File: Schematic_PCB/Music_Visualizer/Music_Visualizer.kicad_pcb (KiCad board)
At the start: 2 copper layers, 295 x 155 mm, 257 parts, among them J1 AudioJack3, J2 PJ-079BH, J3 Screw_Terminal_01x02, Q1 DMP2123LQ-7, SW1 SW_SPDT, SW2 SW_SPST, U1 LM324, U10 LM3915N-1, U11 LM3915N-1, U12 LM3915N-1, U13 LM3915N-1, U14 LM3915N-1, U15 LM3915N-1, U16 LM3915N-1, U17 NCP161ASN350T1G, U18 NCS333ASQ3T2G, U2 LM324, U3 LM324, U4 LM324, U5 LM324, U6 LM324, U7 LM324, U8 LT1054, U9 MC78L05_TO92

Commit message: PCB LEDs placed
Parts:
- removed C1, C2: 47n, Capacitor_SMD:C_0603_1608Metric_Pad1.08x0.95mm_HandSolder
- removed C10, C9: 6.8n, Capacitor_SMD:C_0805_2012Metric
- removed C11, C12: 24n, Capacitor_SMD:C_0805_2012Metric
- removed C13, C14: 4.7n, Capacitor_SMD:C_0603_1608Metric_Pad1.08x0.95mm_HandSolder
- removed C15, C16: 3.3n, Capacitor_SMD:C_0603_1608Metric_Pad1.08x0.95mm_HandSolder
- removed C17, C18: 6.2n, Capacitor_SMD:C_0805_2012Metric
- removed C19, C20: 1.6n, Capacitor_SMD:C_0603_1608Metric_Pad1.08x0.95mm_HandSolder
- removed C21, C22, C25, C26, C27, C28, C29, C30, C31, C32, C33, C34, C35, C36, C37, C38, C41, C42: 1n, Capacitor_SMD:C_0603_1608Metric_Pad1.08x0.95mm_HandSolder
- removed C23, C24: 3n, Capacitor_SMD:C_0603_1608Metric_Pad1.08x0.95mm_HandSolder
- removed C3, C4: 27n, Capacitor_SMD:C_0603_1608Metric_Pad1.08x0.95mm_HandSolder
- removed C39, C40: 820p, Capacitor_SMD:C_0603_1608Metric_Pad1.08x0.95mm_HandSolder
- removed C5, C6: 75n, Capacitor_SMD:C_1206_3216Metric
- removed C59: 10u, Capacitor_THT:CP_Radial_D5.0mm_P2.00mm
- removed C60, C61, C62, C63, C64, C65, C66, C67, C68, C69, C70, C71, C72, C73: 0.1uF, Capacitor_SMD:C_0805_2012Metric
- removed C7, C8: 13n, Capacitor_SMD:C_0805_2012Metric
- removed J2: PJ-079BH, DC_Power_Jack_PJ_070BH:CUI_PJ-079BH
- removed R1: 84.5k, Resistor_SMD:R_0603_1608Metric_Pad0.98x0.95mm_HandSolder
- removed R10: 110k, Resistor_SMD:R_0603_1608Metric_Pad0.98x0.95mm_HandSolder
- removed R11, R4, R65: 90.9k, Resistor_SMD:R_0603_1608Metric_Pad0.98x0.95mm_HandSolder
- removed R12: 162k, Resistor_SMD:R_0603_1608Metric_Pad0.98x0.95mm_HandSolder
- removed R13: 118k, Resistor_SMD:R_0603_1608Metric_Pad0.98x0.95mm_HandSolder
- removed R14: 63.4k, Resistor_SMD:R_0603_1608Metric_Pad0.98x0.95mm_HandSolder
- removed R15: 62k, Resistor_SMD:R_0603_1608Metric_Pad0.98x0.95mm_HandSolder
- removed R16: 309k, Resistor_SMD:R_0603_1608Metric_Pad0.98x0.95mm_HandSolder
- removed R17: 68k, Resistor_SMD:R_0603_1608Metric_Pad0.98x0.95mm_HandSolder
- removed R18, R31, R36, R51: 66.5k, Resistor_SMD:R_0603_1608Metric_Pad0.98x0.95mm_HandSolder
- removed R19: 332k, Resistor_SMD:R_0603_1608Metric_Pad0.98x0.95mm_HandSolder
- removed R2, R41, R50: 160k, Resistor_SMD:R_0603_1608Metric_Pad0.98x0.95mm_HandSolder
- removed R20: 137k, Resistor_SMD:R_0603_1608Metric_Pad0.98x0.95mm_HandSolder
- removed R21: 45.3k, Resistor_SMD:R_0603_1608Metric_Pad0.98x0.95mm_HandSolder
- removed R22, R35, R53: 270k, Resistor_SMD:R_0603_1608Metric_Pad0.98x0.95mm_HandSolder
- removed R23: 143k, Resistor_SMD:R_0603_1608Metric_Pad0.98x0.95mm_HandSolder
- removed R24: 19.1k, Resistor_SMD:R_0603_1608Metric_Pad0.98x0.95mm_HandSolder
- removed R25: 590k, Resistor_SMD:R_0603_1608Metric_Pad0.98x0.95mm_HandSolder
- removed R26: 140k, Resistor_SMD:R_0603_1608Metric_Pad0.98x0.95mm_HandSolder
- removed R27: 18.7k, Resistor_SMD:R_0603_1608Metric_Pad0.98x0.95mm_HandSolder
- removed R28: 576k, Resistor_SMD:R_0603_1608Metric_Pad0.98x0.95mm_HandSolder
- removed R29, R30: 100k, Resistor_SMD:R_0603_1608Metric_Pad0.98x0.95mm_HandSolder
- removed R3: 169k, Resistor_SMD:R_0603_1608Metric_Pad0.98x0.95mm_HandSolder
- removed R32: 33.2k, Resistor_SMD:R_0603_1608Metric_Pad0.98x0.95mm_HandSolder
- removed R33: 56k, Resistor_SMD:R_0603_1608Metric_Pad0.98x0.95mm_HandSolder
- removed R34, R58: 48.7k, Resistor_SMD:R_0603_1608Metric_Pad0.98x0.95mm_HandSolder
- removed R37: 57.6k, Resistor_SMD:R_0603_1608Metric_Pad0.98x0.95mm_HandSolder
- removed R38: 324k, Resistor_SMD:R_0603_1608Metric_Pad0.98x0.95mm_HandSolder
- removed R39, R48: 78.7k, Resistor_SMD:R_0603_1608Metric_Pad0.98x0.95mm_HandSolder
- removed R40: 26.7k, Resistor_SMD:R_0603_1608Metric_Pad0.98x0.95mm_HandSolder
- removed R42: 59k, Resistor_SMD:R_0603_1608Metric_Pad0.98x0.95mm_HandSolder
- removed R43: 7.87k, Resistor_SMD:R_0603_1608Metric_Pad0.98x0.95mm_HandSolder
- removed R44: 243k, Resistor_SMD:R_0603_1608Metric_Pad0.98x0.95mm_HandSolder
- removed R45: 107k, Resistor_SMD:R_0603_1608Metric_Pad0.98x0.95mm_HandSolder
- removed R46: 14.7k, Resistor_SMD:R_0603_1608Metric_Pad0.98x0.95mm_HandSolder
- removed R47: 453k, Resistor_SMD:R_0603_1608Metric_Pad0.98x0.95mm_HandSolder
- removed R49: 7.32k, Resistor_SMD:R_0603_1608Metric_Pad0.98x0.95mm_HandSolder
- removed R5, R62: 37.4k, Resistor_SMD:R_0603_1608Metric_Pad0.98x0.95mm_HandSolder
- removed R52: 2.87k, Resistor_SMD:R_0603_1608Metric_Pad0.98x0.95mm_HandSolder
- removed R54: 95.3k, Resistor_SMD:R_0603_1608Metric_Pad0.98x0.95mm_HandSolder
- removed R55: 4.02k, Resistor_SMD:R_0603_1608Metric_Pad0.98x0.95mm_HandSolder
- removed R56: 383k, Resistor_SMD:R_0603_1608Metric_Pad0.98x0.95mm_HandSolder
- removed R57: 11.5k, Resistor_SMD:R_0805_2012Metric
- removed R59: 22.6k, Resistor_SMD:R_0603_1608Metric_Pad0.98x0.95mm_HandSolder
- removed R6: 402k, Resistor_SMD:R_0603_1608Metric_Pad0.98x0.95mm_HandSolder
- removed R60: 8.06k, Resistor_SMD:R_0603_1608Metric_Pad0.98x0.95mm_HandSolder
- removed R61: 4.32k, Resistor_SMD:R_0603_1608Metric_Pad0.98x0.95mm_HandSolder
- removed R63: 19.6k, Resistor_SMD:R_0603_1608Metric_Pad0.98x0.95mm_HandSolder
- removed R64: 10.7k, Resistor_SMD:R_0603_1608Metric_Pad0.98x0.95mm_HandSolder
- removed R7: 86.6k, Resistor_SMD:R_0603_1608Metric_Pad0.98x0.95mm_HandSolder
- removed R8: 35.7k, Resistor_SMD:R_0603_1608Metric_Pad0.98x0.95mm_HandSolder
- removed R9: 390k, Resistor_SMD:R_0603_1608Metric_Pad0.98x0.95mm_HandSolder
- removed U17: NCP161ASN350T1G, Package_TO_SOT_SMD:SOT-23-5
- removed U18: NCS333ASQ3T2G, Package_TO_SOT_SMD:SOT-353_SC-70-5
- added J4: NMJ4HCD2, Connector_Audio:Jack_6.35mm_Neutrik_NMJ4HCD2_Horizontal, F.Cu at (297.0, 211.7)
- added J5: Screw_Terminal_01x02, TerminalBlock_Phoenix:TerminalBlock_Phoenix_MPT-0,5-2-2.54_1x02_P2.54mm_Horizontal, F.Cu at (81.0, 201.8)
- added J6: 3.5mm, PCM_SparkFun-Connector:ScrewTerminal_1x03_P3.5mm_Horizontal_Black, F.Cu at (97.5, 210.4)
- added J7: Barrel_Jack_PTH_Slot, PCM_SparkFun-Connector:Barrel_Jack_PTH_Slot, F.Cu at (301.5, 183.5)
- added R83: 10k, Resistor_SMD:R_0805_2012Metric_Pad1.20x1.40mm_HandSolder, F.Cu at (97.0, 217.1)
- added R84: 10k, Resistor_SMD:R_0805_2012Metric_Pad1.20x1.40mm_HandSolder, F.Cu at (97.0, 220.0)
- added TP1: T_SB, Custom_Footprints:TEST1Y, F.Cu at (91.3, 181.1)
- added TP10: T_pw, Custom_Footprints:TEST1Y, F.Cu at (91.3, 209.5)
- added TP11: T_mid, Custom_Footprints:TEST1Y, F.Cu at (91.3, 216.1)
- added TP12: T_ref, Custom_Footprints:TEST1Y, F.Cu at (53.2, 225.7)
- added TP13: T_grnd, Custom_Footprints:TEST1Y, F.Cu at (91.3, 222.7)
- added TP14: T_a_out, Custom_Footprints:TEST1Y, F.Cu at (81.7, 194.3)
- added TP2: T_B, Custom_Footprints:TEST1Y, F.Cu at (91.3, 187.7)
- added TP3: T_LM, Custom_Footprints:TEST1Y, F.Cu at (91.3, 194.3)
- added TP4: T_M, Custom_Footprints:TEST1Y, F.Cu at (91.3, 200.9)
- added TP5: T_UM, Custom_Footprints:TEST1Y, F.Cu at (97.9, 181.1)
- added TP6: V_MH, Custom_Footprints:TEST1Y, F.Cu at (97.9, 187.7)
- added TP7: V_H, Custom_Footprints:TEST1Y, F.Cu at (97.9, 194.3)
- added TP8: T_a_in, Custom_Footprints:TEST1Y, F.Cu at (81.7, 181.1)
- added TP9: T_sig, Custom_Footprints:TEST1Y, F.Cu at (81.7, 187.7)
- C43: value 100u -> 10u; footprint Capacitor_SMD:C_1206_3216Metric -> Capacitor_SMD:C_0805_2012Metric_Pad1.18x1.45mm_HandSolder; moved to B.Cu
- C44: value 100u -> 4.7n; footprint Capacitor_SMD:C_1206_3216Metric -> Capacitor_SMD:C_0805_2012Metric_Pad1.18x1.45mm_HandSolder
- C45: value 10u -> 4.7n; footprint Capacitor_SMD:C_0805_2012Metric -> Capacitor_SMD:C_0805_2012Metric_Pad1.18x1.45mm_HandSolder
- C46: value 10u -> 1u; footprint Capacitor_SMD:C_0805_2012Metric -> Capacitor_SMD:C_0805_2012Metric_Pad1.18x1.45mm_HandSolder; moved to B.Cu
- C47, C48, C49: value 1u -> 2.2n; footprint Capacitor_SMD:C_0603_1608Metric_Pad1.08x0.95mm_HandSolder -> Capacitor_SMD:C_0805_2012Metric_Pad1.18x1.45mm_HandSolder; moved to B.Cu
- C50: value 0.33uF -> 2.2n; footprint Capacitor_SMD:C_0603_1608Metric_Pad1.08x0.95mm_HandSolder -> Capacitor_SMD:C_0805_2012Metric_Pad1.18x1.45mm_HandSolder
- C51: value 0.1uF -> 2.2n; footprint Capacitor_SMD:C_0805_2012Metric -> Capacitor_SMD:C_0805_2012Metric_Pad1.18x1.45mm_HandSolder
- C52: value 1u -> 2.2n; footprint Capacitor_SMD:C_0603_1608Metric_Pad1.08x0.95mm_HandSolder -> Capacitor_SMD:C_0805_2012Metric_Pad1.18x1.45mm_HandSolder
- C53: footprint Capacitor_SMD:C_0603_1608Metric_Pad1.08x0.95mm_HandSolder -> Capacitor_SMD:C_0805_2012Metric_Pad1.18x1.45mm_HandSolder
- C54: value 10u -> 47u; footprint Capacitor_SMD:C_0805_2012Metric -> Capacitor_THT:CP_Radial_D5.0mm_P2.00mm
- C55: value 100u -> 100n; footprint Capacitor_THT:C_Radial_D5.0mm_H5.0mm_P2.00mm -> Capacitor_SMD:C_0805_2012Metric_Pad1.18x1.45mm_HandSolder
- C56: value 0.002u -> 100n; footprint Capacitor_SMD:C_0603_1608Metric_Pad1.08x0.95mm_HandSolder -> Capacitor_SMD:C_0805_2012Metric_Pad1.18x1.45mm_HandSolder
- C57, C58: value 1u -> 10u; footprint Capacitor_SMD:C_0603_1608Metric_Pad1.08x0.95mm_HandSolder -> Capacitor_THT:CP_Radial_D5.0mm_P2.00mm
- D1, D10, D11, D12, D13, D14, D15, D16, D17, D18, D19, D2, D20, D21, D22, D23, D24, D25, D26, D27, D28, D29, D3, D30, D31, D32, D33, D34, D35, D36, D37, D38, D39, D4, D40, D41, D42, D43, D44, D45, D46, D47, D48, D49, D5, D50, D51, D52, D53, D54, D55, D56, D57, D58, D59, D6, D60, D61, D62, D63, D64, D65, D66, D67, D68, D69, D7, D70, D71, D8, D9: footprint LED_THT:LED_D5.0mm -> LED_SMD:LED_1210_3225Metric_Pad1.42x2.65mm_HandSolder
- J1: value AudioJack3 -> NMJ4HCD2; footprint Connector_Audio:Jack_3.5mm_CUI_SJ-3523-SMT_Horizontal -> Connector_Audio:Jack_6.35mm_Neutrik_NMJ4HCD2_Horizontal; moved to B.Cu
- R66, R75, R76, R77, R78, R79, R80, R81: footprint Resistor_SMD:R_0603_1608Metric_Pad0.98x0.95mm_HandSolder -> Resistor_SMD:R_0805_2012Metric_Pad1.20x1.40mm_HandSolder; moved to B.Cu
- R67: value 1k -> 3.3k; footprint Resistor_SMD:R_0603_1608Metric_Pad0.98x0.95mm_HandSolder -> Resistor_SMD:R_0805_2012Metric_Pad1.20x1.40mm_HandSolder
- R68: value 1k -> 1.6k; footprint Resistor_SMD:R_0603_1608Metric_Pad0.98x0.95mm_HandSolder -> Resistor_SMD:R_0805_2012Metric_Pad1.20x1.40mm_HandSolder
- R69: value 1k -> 15k; footprint Resistor_SMD:R_0603_1608Metric_Pad0.98x0.95mm_HandSolder -> Resistor_SMD:R_0805_2012Metric_Pad1.20x1.40mm_HandSolder; moved to B.Cu
- R70: value 1k -> 5.6k; footprint Resistor_SMD:R_0603_1608Metric_Pad0.98x0.95mm_HandSolder -> Resistor_SMD:R_0805_2012Metric_Pad1.20x1.40mm_HandSolder; moved to B.Cu
- R71: value 1k -> 22k; footprint Resistor_SMD:R_0603_1608Metric_Pad0.98x0.95mm_HandSolder -> Resistor_SMD:R_0805_2012Metric_Pad1.20x1.40mm_HandSolder; moved to B.Cu
- R72: value 1k -> 10k; footprint Resistor_SMD:R_0603_1608Metric_Pad0.98x0.95mm_HandSolder -> Resistor_SMD:R_0805_2012Metric_Pad1.20x1.40mm_HandSolder; moved to B.Cu
- R73: value 20k -> 1k; footprint Resistor_SMD:R_0603_1608Metric_Pad0.98x0.95mm_HandSolder -> Resistor_SMD:R_0805_2012Metric_Pad1.20x1.40mm_HandSolder
- R74: value 102k -> 10k; footprint Resistor_SMD:R_0603_1608Metric_Pad0.98x0.95mm_HandSolder -> Resistor_SMD:R_0805_2012Metric_Pad1.20x1.40mm_HandSolder
- R82: footprint Resistor_SMD:R_0603_1608Metric_Pad0.98x0.95mm_HandSolder -> Resistor_SMD:R_0805_2012Metric_Pad1.20x1.40mm_HandSolder
- RV2: value 5k_Rhi_Adjuster -> 1k_Rhi_Adjuster
- SW1: value SW_SPDT -> SW_Slide_DPDT; footprint Slide_Switch:SW_OS102011MS2QN1 -> Button_Switch_THT:SW_CK_JS202011CQN_DPDT_Straight
- SW2: footprint PW_On_Off_Switch:E-SWITCH_RR511D1121 -> Button_Switch_THT:SW_Slide-03_Wuerth-WS-SLTV_10x2.5x6.4_P2.54mm
- U8: value LT1054 -> LM324; footprint LT1054_PDIP_Lin_Reg:DIP794W45P254L959H508Q8 -> Package_SO:SOIC-14_3.9x8.7mm_P1.27mm
- U9: value MC78L05_TO92 -> LM324; footprint Package_TO_SOT_THT:TO-92_Inline -> Package_SO:SOIC-14_3.9x8.7mm_P1.27mm
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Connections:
- C44 pad 1: Net-(C11-Pad2) (its old number) -> Net-(C44-Pad1)
- C44 pad 2: VBass -> Net-(C44-Pad2)
- C45 pad 1: Net-(C17-Pad2) -> Net-(C44-Pad1)
- C45 pad 2: VLowerMidrange -> Net-(U8C--)
- C46 pad 1: Net-(C23-Pad2) -> Net-(C44-Pad2)
- C46 pad 2: VMidrange -> VPresence
- C47 pad 1: Net-(C29-Pad2) -> Net-(C47-Pad1)
- C47 pad 2: VUpperMidrange -> Net-(C47-Pad2)
- C48 pad 1: Net-(C35-Pad2) -> Net-(C47-Pad1)
- C48 pad 2: VPresence -> Net-(U9A--)
- C49 pad 1: Net-(C41-Pad2) -> Net-(C49-Pad1)
- C49 pad 2: VBrilliance -> Net-(C49-Pad2)
- C50 pad 1: +9V -> Net-(C49-Pad1)
- C50 pad 2: GND -> Net-(U9B--)
- C51 pad 1: +5V -> Net-(C51-Pad1)
- C51 pad 2: GND -> Net-(C51-Pad2)
- C52 pad 1: +9V -> Net-(C51-Pad1)
- C52 pad 2: GND -> Net-(U9C--)
- C53 pad 1: +9V -> Net-(C51-Pad2)
- C53 pad 2: GND -> VBrilliance
- C54 pad 1: Net-(C54-Pad1) -> VCC4_5
- C54 pad 2: Net-(C54-Pad2) -> GND
- C55 pad 2: -5V -> VCC4_5
- C56 pad 1: -5V -> GND
- C56 pad 2: Net-(C56-Pad2) -> Rhi_Value
- C57 pad 1: +5V -> Rhi_Value
- C58 pad 1: /LED_Driver/3.5V -> +9V
- J1 pad T: /Vsig_female -> Net-(C8-Pad1)
- J3 pad 1: GND -> Net-(J3-Pin_1)
- J3 pad 2: /Vsig_male -> GND
- Q1 pad 1: /Power/Power -> Net-(Q1-D)
- R67 pad 1: VBass -> Net-(C47-Pad2)
- R67 pad 2: GND -> Net-(C49-Pad1)
- R68 pad 1: VLowerMidrange -> Net-(C49-Pad1)
- R68 pad 2: GND -> VCC4_5
- R69 pad 1: VMidrange -> Net-(C49-Pad2)
- R69 pad 2: GND -> Net-(U9B--)
- R70 pad 1: VUpperMidrange -> Net-(C49-Pad2)
- R70 pad 2: GND -> Net-(C51-Pad1)
- R71 pad 1: VPresence -> Net-(C51-Pad1)
- R71 pad 2: GND -> VCC4_5
- R72 pad 1: VBrilliance -> Net-(C51-Pad2)
- R72 pad 2: GND -> Net-(U9C--)
- R73 pad 1: Net-(C56-Pad2) -> VBrilliance
- R73 pad 2: Net-(R73-Pad2) -> GND
- R74 pad 1: -5V -> +9V
- R74 pad 2: Net-(C56-Pad2) -> Rhi_Value
- RV2 pad 1: GND -> unconnected-(RV2-Pad1)
- RV2 pad 2: Net-(RV2-Pad2) -> GND
- RV2 pad 3: /LED_Driver/3.5V -> Rhi_Value
- SW1 pad 1: /Vsig_male -> unconnected-(SW1-A-Pad1)
- SW1 pad 2: Vsig -> unconnected-(SW1-B-Pad2)
- SW1 pad 3: /Vsig_female -> unconnected-(SW1-C-Pad3)
- U1 pad 10: GND -> VCC4_5
- U1 pad 11: -5V -> GND
- U1 pad 3: GND -> VCC4_5
- U1 pad 4: +5V -> +9V
- U1 pad 5: GND -> VCC4_5
- U2 pad 1: Net-(C7-Pad2) -> (no net)
- U2 pad 10: GND -> (no net)
- U2 pad 11: -5V -> GND
- U2 pad 12: Vsig -> Net-(U2D-+)
- U2 pad 2: Net-(C8-Pad2) -> (no net)
- U2 pad 3: Net-(R12-Pad2) -> (no net)
- U2 pad 4: +5V -> +9V
- U2 pad 5: GND -> (no net)
- U2 pad 6: Net-(C10-Pad2) -> (no net)
- U2 pad 7: Net-(C9-Pad2) -> (no net)
- U2 pad 8: Net-(C11-Pad2) (its old number) -> (no net)
- U2 pad 9: Net-(C12-Pad2) -> (no net)
- U3 pad 1: Net-(C13-Pad2) (its old number) -> (no net)
- U3 pad 10: GND -> (no net)
- U3 pad 11: -5V -> GND
- U3 pad 12: Vsig -> Net-(U3D-+)
- U3 pad 2: Net-(C14-Pad2) -> (no net)
- U3 pad 3: GND -> (no net)
- U3 pad 4: +5V -> +9V
- U3 pad 5: GND -> (no net)
- U3 pad 6: Net-(C16-Pad2) -> (no net)
- U3 pad 7: Net-(C15-Pad2) -> (no net)
- U3 pad 8: Net-(C17-Pad2) -> (no net)
- U3 pad 9: Net-(C18-Pad2) (its old number) -> (no net)
- U4 pad 10: GND -> VCC4_5
- U4 pad 11: -5V -> GND
- U4 pad 3: Net-(R31-Pad2) -> VCC4_5
- U4 pad 4: +5V -> +9V
- U4 pad 5: GND -> VCC4_5
- U4 pad 8: Net-(C23-Pad2) -> Net-(C15-Pad2)
- U5 pad 10: GND -> VCC4_5
- U5 pad 11: -5V -> GND
- U5 pad 3: GND -> VCC4_5
- U5 pad 4: +5V -> +9V
- U5 pad 5: GND -> VCC4_5
- U5 pad 8: Net-(C29-Pad2) -> Net-(C22-Pad2)
- U6 pad 10: GND -> VCC4_5
- U6 pad 11: -5V -> GND
- U6 pad 3: GND -> VCC4_5
- U6 pad 4: +5V -> +9V
- U6 pad 5: GND -> VCC4_5
- U6 pad 8: Net-(C35-Pad2) -> Net-(C29-Pad2)
- U7 pad 10: GND -> VCC4_5
- U7 pad 3: GND -> VCC4_5
- U7 pad 4: +5V -> +9V
- U7 pad 5: GND -> VCC4_5
- U7 pad 8: Net-(C41-Pad2) -> Net-(C36-Pad2)
- U8 pad 1: Net-(C56-Pad2) -> Net-(C39-Pad2)
- U8 pad 2: Net-(C54-Pad1) -> Net-(U8A--)
- U8 pad 3: GND -> VCC4_5
- U8 pad 4: Net-(C54-Pad2) -> (no net)
- U8 pad 5: -5V -> VCC4_5
- U8 pad 6: Net-(R73-Pad2) -> Net-(U8B--)
- U8 pad 7: unconnected-(U8-Pad7) -> Net-(C41-Pad2)
- U8 pad 8: +9V -> Net-(C44-Pad2)
- U9 pad 1: +5V -> Net-(C47-Pad2)
- U9 pad 2: GND -> Net-(U9A--)
- U9 pad 3: +9V -> VCC4_5
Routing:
- net +9V: track 1202.9 -> 379.7 mm
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- removed copper zone on B.Cu, net GND
- removed copper zone on F.Cu, net GND
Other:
- board text added: "Bass [60Hz:150Hz]"
- board text added: "Low Midrange [150Hz:400Hz]"
- board text added: "Midrange [400Hz:1kHz]"
- board text added: "Presence [2.5kHz:6kHz]"
- board text added: "Upper-Midrange [1kHz:2.5kHz]"
- board text removed: "Bass [60Hz:250Hz]"
- board text removed: "Jack Source"
- board text removed: "Low-Midrange [250Hz:500Hz]"
- board text removed: "Midrange [500Hz:2kHz]"
- board text removed: "Plug Source"
- board text removed: "Presence [4kHz:6kHz]"
- board text removed: "Upper-Midrange [2kHz:4kHz]"

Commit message: Battery low
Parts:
- removed J7: Barrel_Jack_PTH_Slot, PCM_SparkFun-Connector:Barrel_Jack_PTH_Slot
- removed U9: LM324, Package_SO:SOIC-14_3.9x8.7mm_P1.27mm
- added C1: 220n, Capacitor_SMD:C_0805_2012Metric_Pad1.18x1.45mm_HandSolder, F.Cu at (38.9, 118.1)
- added C10: 10u, Capacitor_THT:CP_Radial_D5.0mm_P2.00mm, F.Cu at (73.7, 277.3)
- added C11: 100n, Capacitor_SMD:C_0805_2012Metric_Pad1.18x1.45mm_HandSolder, F.Cu at (32.0, 151.7)
- added C12: 100n, Capacitor_SMD:C_0805_2012Metric_Pad1.18x1.45mm_HandSolder, F.Cu at (32.0, 154.8)
- added C13: 100n, Capacitor_SMD:C_0805_2012Metric_Pad1.18x1.45mm_HandSolder, F.Cu at (43.3, 275.4)
- added C14: 100n, Capacitor_SMD:C_0805_2012Metric_Pad1.18x1.45mm_HandSolder, F.Cu at (43.3, 278.4)
- added C15: 100n, Capacitor_SMD:C_0805_2012Metric_Pad1.18x1.45mm_HandSolder, F.Cu at (43.3, 281.4)
- added C16: 100n, Capacitor_SMD:C_0805_2012Metric_Pad1.18x1.45mm_HandSolder, F.Cu at (43.3, 284.5)
- added C17: 10u, Capacitor_SMD:C_0805_2012Metric_Pad1.18x1.45mm_HandSolder, F.Cu at (43.3, 287.5)
- added C18: 47n, Capacitor_SMD:C_0805_2012Metric_Pad1.18x1.45mm_HandSolder, F.Cu at (43.3, 290.5)
- added C19: 47n, Capacitor_SMD:C_0805_2012Metric_Pad1.18x1.45mm_HandSolder, F.Cu at (43.3, 293.5)
- added C2: 220n, Capacitor_SMD:C_0805_2012Metric_Pad1.18x1.45mm_HandSolder, F.Cu at (38.9, 120.1)
- added C20: 47n, Capacitor_SMD:C_0805_2012Metric_Pad1.18x1.45mm_HandSolder, F.Cu at (43.3, 296.5)
- added C21: 47n, Capacitor_SMD:C_0805_2012Metric_Pad1.18x1.45mm_HandSolder, F.Cu at (48.2, 275.4)
- added C22: 47n, Capacitor_SMD:C_0805_2012Metric_Pad1.18x1.45mm_HandSolder, F.Cu at (48.2, 278.4)
- added C23: 47n, Capacitor_SMD:C_0805_2012Metric_Pad1.18x1.45mm_HandSolder, F.Cu at (48.2, 281.4)
- added C24: 10u, Capacitor_SMD:C_0805_2012Metric_Pad1.18x1.45mm_HandSolder, F.Cu at (48.2, 284.5)
- added C25: 22n, Capacitor_SMD:C_0805_2012Metric_Pad1.18x1.45mm_HandSolder, F.Cu at (48.2, 287.5)
- added C26: 22n, Capacitor_SMD:C_0805_2012Metric_Pad1.18x1.45mm_HandSolder, F.Cu at (48.2, 290.5)
- added C27: 22n, Capacitor_SMD:C_0805_2012Metric_Pad1.18x1.45mm_HandSolder, F.Cu at (48.2, 293.5)
- added C28: 22n, Capacitor_SMD:C_0805_2012Metric_Pad1.18x1.45mm_HandSolder, F.Cu at (48.2, 296.5)
- added C29: 22n, Capacitor_SMD:C_0805_2012Metric_Pad1.18x1.45mm_HandSolder, F.Cu at (53.0, 275.4)
- added C3: 220n, Capacitor_SMD:C_0805_2012Metric_Pad1.18x1.45mm_HandSolder, F.Cu at (46.8, 120.2)
- added C30: 22n, Capacitor_SMD:C_0805_2012Metric_Pad1.18x1.45mm_HandSolder, F.Cu at (53.0, 278.4)
- added C31: 1u, Capacitor_SMD:C_0805_2012Metric_Pad1.18x1.45mm_HandSolder, F.Cu at (53.0, 281.4)
- added C32: 10n, Capacitor_SMD:C_0805_2012Metric_Pad1.18x1.45mm_HandSolder, F.Cu at (53.0, 284.5)
- added C33: 10n, Capacitor_SMD:C_0805_2012Metric_Pad1.18x1.45mm_HandSolder, F.Cu at (53.0, 287.5)
- added C34: 10n, Capacitor_SMD:C_0805_2012Metric_Pad1.18x1.45mm_HandSolder, F.Cu at (53.0, 290.5)
- added C35: 10n, Capacitor_SMD:C_0805_2012Metric_Pad1.18x1.45mm_HandSolder, F.Cu at (53.0, 293.5)
- added C36: 10n, Capacitor_SMD:C_0805_2012Metric_Pad1.18x1.45mm_HandSolder, F.Cu at (53.0, 296.5)
- added C37: 10n, Capacitor_SMD:C_0805_2012Metric_Pad1.18x1.45mm_HandSolder, F.Cu at (57.8, 275.4)
- added C38: 1u, Capacitor_SMD:C_0805_2012Metric_Pad1.18x1.45mm_HandSolder, F.Cu at (57.8, 278.4)
- added C39: 4.7n, Capacitor_SMD:C_0805_2012Metric_Pad1.18x1.45mm_HandSolder, F.Cu at (57.8, 281.4)
- added C4: 220n, Capacitor_SMD:C_0805_2012Metric_Pad1.18x1.45mm_HandSolder, F.Cu at (48.8, 120.2)
- added C40: 4.7n, Capacitor_SMD:C_0805_2012Metric_Pad1.18x1.45mm_HandSolder, F.Cu at (57.8, 284.5)
- added C41: 4.7n, Capacitor_SMD:C_0805_2012Metric_Pad1.18x1.45mm_HandSolder, F.Cu at (57.8, 287.5)
- added C42: 4.7n, Capacitor_SMD:C_0805_2012Metric_Pad1.18x1.45mm_HandSolder, F.Cu at (57.8, 290.5)
- added C5: 220n, Capacitor_SMD:C_0805_2012Metric_Pad1.18x1.45mm_HandSolder, F.Cu at (42.5, 124.2)
- added C59: 100n, Capacitor_SMD:C_0805_2012Metric_Pad1.18x1.45mm_HandSolder, F.Cu at (73.8, 248.9)
- added C6: 220n, Capacitor_SMD:C_0805_2012Metric_Pad1.18x1.45mm_HandSolder, F.Cu at (44.5, 124.2)
- added C60: 100n, Capacitor_SMD:C_0805_2012Metric_Pad1.18x1.45mm_HandSolder, F.Cu at (73.8, 251.9)
- added C61: 100n, Capacitor_SMD:C_0805_2012Metric_Pad1.18x1.45mm_HandSolder, F.Cu at (73.8, 254.9)
- added C62: 100n, Capacitor_SMD:C_0805_2012Metric_Pad1.18x1.45mm_HandSolder, F.Cu at (73.8, 257.9)
- added C63: 100n, Capacitor_SMD:C_0805_2012Metric_Pad1.18x1.45mm_HandSolder, F.Cu at (73.8, 260.9)
- added C64: 100n, Capacitor_SMD:C_0805_2012Metric_Pad1.18x1.45mm_HandSolder, F.Cu at (73.8, 263.9)
- added C65: 100n, Capacitor_SMD:C_0805_2012Metric_Pad1.18x1.45mm_HandSolder, F.Cu at (78.6, 248.9)
- added C66: 100n, Capacitor_SMD:C_0805_2012Metric_Pad1.18x1.45mm_HandSolder, F.Cu at (78.6, 251.9)
- added C67: 100n, Capacitor_SMD:C_0805_2012Metric_Pad1.18x1.45mm_HandSolder, F.Cu at (78.6, 254.9)
- added C68: 100n, Capacitor_SMD:C_0805_2012Metric_Pad1.18x1.45mm_HandSolder, F.Cu at (78.6, 257.9)
- added C69: 100n, Capacitor_SMD:C_0805_2012Metric_Pad1.18x1.45mm_HandSolder, F.Cu at (78.6, 260.9)
- added C7: 100n, Capacitor_SMD:C_0805_2012Metric_Pad1.18x1.45mm_HandSolder, F.Cu at (80.4, 268.9)
- added C70: 100n, Capacitor_SMD:C_0805_2012Metric_Pad1.18x1.45mm_HandSolder, F.Cu at (78.6, 263.9)
- added C71: 100n, Capacitor_SMD:C_0805_2012Metric_Pad1.18x1.45mm_HandSolder, F.Cu at (83.4, 248.9)
- added C72: 100n, Capacitor_SMD:C_0805_2012Metric_Pad1.18x1.45mm_HandSolder, F.Cu at (83.4, 251.9)
- added C73: 100n, Capacitor_SMD:C_0805_2012Metric_Pad1.18x1.45mm_HandSolder, F.Cu at (83.4, 254.9)
- added C74: 100n, Capacitor_SMD:C_0805_2012Metric_Pad1.18x1.45mm_HandSolder, F.Cu at (83.4, 257.9)
- added C8: 10u, Capacitor_THT:CP_Radial_D5.0mm_P2.00mm, F.Cu at (73.7, 270.7)
- added C9: 100n, Capacitor_SMD:C_0805_2012Metric_Pad1.18x1.45mm_HandSolder, F.Cu at (80.4, 271.9)
- added J2: Barrel_Jack_PTH, Custom_Footprints:RAPC722X, B.Cu at (60.1, 94.3)
- added R1: 27k, Resistor_SMD:R_0805_2012Metric_Pad1.20x1.40mm_HandSolder, F.Cu at (38.9, 116.1)
- added R10: 1m, Resistor_SMD:R_0805_2012Metric_Pad1.20x1.40mm_HandSolder, F.Cu at (80.4, 274.9)
- added R11: 1m, Resistor_SMD:R_0805_2012Metric_Pad1.20x1.40mm_HandSolder, F.Cu at (80.4, 277.9)
- added R12: 100k, Resistor_SMD:R_0805_2012Metric_Pad1.20x1.40mm_HandSolder, F.Cu at (80.4, 280.8)
- added R13: 27k, Resistor_SMD:R_0805_2012Metric_Pad1.20x1.40mm_HandSolder, F.Cu at (43.3, 248.8)
- added R14: 6.8k, Resistor_SMD:R_0805_2012Metric_Pad1.20x1.40mm_HandSolder, F.Cu at (43.3, 251.8)
- added R15: 120k, Resistor_SMD:R_0805_2012Metric_Pad1.20x1.40mm_HandSolder, F.Cu at (43.3, 254.8)
- added R16: 12k, Resistor_SMD:R_0805_2012Metric_Pad1.20x1.40mm_HandSolder, F.Cu at (43.3, 257.7)
- added R17: 3.3k, Resistor_SMD:R_0805_2012Metric_Pad1.20x1.40mm_HandSolder, F.Cu at (43.3, 260.6)
- added R18: 56k, Resistor_SMD:R_0805_2012Metric_Pad1.20x1.40mm_HandSolder, F.Cu at (43.3, 263.6)
- added R19: 18k, Resistor_SMD:R_0805_2012Metric_Pad1.20x1.40mm_HandSolder, F.Cu at (43.3, 266.6)
- added R2: 12k, Resistor_SMD:R_0805_2012Metric_Pad1.20x1.40mm_HandSolder, F.Cu at (42.9, 116.1)
- added R20: 15k, Resistor_SMD:R_0805_2012Metric_Pad1.20x1.40mm_HandSolder, F.Cu at (43.3, 269.5)
- added R21: 39k, Resistor_SMD:R_0805_2012Metric_Pad1.20x1.40mm_HandSolder, F.Cu at (43.3, 272.4)
- added R22: 1k, Resistor_SMD:R_0805_2012Metric_Pad1.20x1.40mm_HandSolder, F.Cu at (48.0, 248.8)
- added R23: 22k, Resistor_SMD:R_0805_2012Metric_Pad1.20x1.40mm_HandSolder, F.Cu at (48.0, 251.8)
- added R24: 6.8k, Resistor_SMD:R_0805_2012Metric_Pad1.20x1.40mm_HandSolder, F.Cu at (48.0, 254.8)
- added R25: 100k, Resistor_SMD:R_0805_2012Metric_Pad1.20x1.40mm_HandSolder, F.Cu at (48.0, 257.7)
- added R26: 8.2, Resistor_SMD:R_0805_2012Metric_Pad1.20x1.40mm_HandSolder, F.Cu at (48.0, 260.6)
- added R27: 2.7k, Resistor_SMD:R_0805_2012Metric_Pad1.20x1.40mm_HandSolder, F.Cu at (48.0, 263.6)
- added R28: 39k, Resistor_SMD:R_0805_2012Metric_Pad1.20x1.40mm_HandSolder, F.Cu at (48.0, 266.6)
- added R29: 15k, Resistor_SMD:R_0805_2012Metric_Pad1.20x1.40mm_HandSolder, F.Cu at (48.0, 269.5)
- added R3: 150k, Resistor_SMD:R_0805_2012Metric_Pad1.20x1.40mm_HandSolder, F.Cu at (43.9, 120.1)
- added R30: 15k, Resistor_SMD:R_0805_2012Metric_Pad1.20x1.40mm_HandSolder, F.Cu at (48.0, 272.4)
- added R31: 27k, Resistor_SMD:R_0805_2012Metric_Pad1.20x1.40mm_HandSolder, F.Cu at (52.8, 248.8)
- added R32: 1k, Resistor_SMD:R_0805_2012Metric_Pad1.20x1.40mm_HandSolder, F.Cu at (52.8, 251.8)
- added R33: 18k, Resistor_SMD:R_0805_2012Metric_Pad1.20x1.40mm_HandSolder, F.Cu at (52.8, 254.8)
- added R34: 4.7k, Resistor_SMD:R_0805_2012Metric_Pad1.20x1.40mm_HandSolder, F.Cu at (52.8, 257.7)
- added R35: 82k, Resistor_SMD:R_0805_2012Metric_Pad1.20x1.40mm_HandSolder, F.Cu at (52.8, 260.6)
- added R36: 8.2k, Resistor_SMD:R_0805_2012Metric_Pad1.20x1.40mm_HandSolder, F.Cu at (52.8, 263.6)
- added R37: 2.2k, Resistor_SMD:R_0805_2012Metric_Pad1.20x1.40mm_HandSolder, F.Cu at (52.8, 266.6)
- added R38: 33k, Resistor_SMD:R_0805_2012Metric_Pad1.20x1.40mm_HandSolder, F.Cu at (52.8, 269.5)
- added R39: 12k, Resistor_SMD:R_0805_2012Metric_Pad1.20x1.40mm_HandSolder, F.Cu at (52.8, 272.4)
- added R4: 10k, Resistor_SMD:R_0805_2012Metric_Pad1.20x1.40mm_HandSolder, F.Cu at (43.9, 118.1)
- added R40: 10k, Resistor_SMD:R_0805_2012Metric_Pad1.20x1.40mm_HandSolder, F.Cu at (57.5, 248.8)
- added R41: 27k, Resistor_SMD:R_0805_2012Metric_Pad1.20x1.40mm_HandSolder, F.Cu at (57.5, 251.8)
- added R42: 1k, Resistor_SMD:R_0805_2012Metric_Pad1.20x1.40mm_HandSolder, F.Cu at (57.5, 254.8)
- added R43: 15k, Resistor_SMD:R_0805_2012Metric_Pad1.20x1.40mm_HandSolder, F.Cu at (57.5, 257.7)
- added R44: 4.7k, Resistor_SMD:R_0805_2012Metric_Pad1.20x1.40mm_HandSolder, F.Cu at (57.5, 260.6)
- added R45: 68k, Resistor_SMD:R_0805_2012Metric_Pad1.20x1.40mm_HandSolder, F.Cu at (57.5, 263.6)
- added R46: 6.8k, Resistor_SMD:R_0805_2012Metric_Pad1.20x1.40mm_HandSolder, F.Cu at (57.5, 266.6)
- added R47: 1.8k, Resistor_SMD:R_0805_2012Metric_Pad1.20x1.40mm_HandSolder, F.Cu at (57.5, 269.5)
- added R48: 33k, Resistor_SMD:R_0805_2012Metric_Pad1.20x1.40mm_HandSolder, F.Cu at (57.5, 272.4)
- added R49: 10k, Resistor_SMD:R_0805_2012Metric_Pad1.20x1.40mm_HandSolder, F.Cu at (62.3, 248.8)
- added R5: 4.7k, Resistor_SMD:R_0805_2012Metric_Pad1.20x1.40mm_HandSolder, F.Cu at (46.9, 116.1)
- added R50: 8.2, Resistor_SMD:R_0805_2012Metric_Pad1.20x1.40mm_HandSolder, F.Cu at (62.3, 251.8)
- added R51: 22k, Resistor_SMD:R_0805_2012Metric_Pad1.20x1.40mm_HandSolder, F.Cu at (62.3, 254.8)
- added R52: 1k, Resistor_SMD:R_0805_2012Metric_Pad1.20x1.40mm_HandSolder, F.Cu at (62.3, 257.7)
- added R53: 15k, Resistor_SMD:R_0805_2012Metric_Pad1.20x1.40mm_HandSolder, F.Cu at (62.3, 260.6)
- added R54: 3.3k, Resistor_SMD:R_0805_2012Metric_Pad1.20x1.40mm_HandSolder, F.Cu at (62.3, 263.6)
- added R55: 56k, Resistor_SMD:R_0805_2012Metric_Pad1.20x1.40mm_HandSolder, F.Cu at (62.3, 266.6)
- added R56: 6.8k, Resistor_SMD:R_0805_2012Metric_Pad1.20x1.40mm_HandSolder, F.Cu at (62.3, 269.5)
- added R57: 1.5k, Resistor_SMD:R_0805_2012Metric_Pad1.20x1.40mm_HandSolder, F.Cu at (62.3, 272.4)
- added R58: 27k, Resistor_SMD:R_0805_2012Metric_Pad1.20x1.40mm_HandSolder, F.Cu at (67.0, 248.8)
- added R59: 10k, Resistor_SMD:R_0805_2012Metric_Pad1.20x1.40mm_HandSolder, F.Cu at (67.0, 251.8)
- added R6: 47k, Resistor_SMD:R_0805_2012Metric_Pad1.20x1.40mm_HandSolder, F.Cu at (36.6, 124.2)
- added R60: 6.8k, Resistor_SMD:R_0805_2012Metric_Pad1.20x1.40mm_HandSolder, F.Cu at (67.0, 254.8)
- added R61: 22k, Resistor_SMD:R_0805_2012Metric_Pad1.20x1.40mm_HandSolder, F.Cu at (67.0, 257.7)
- added R62: 1k, Resistor_SMD:R_0805_2012Metric_Pad1.20x1.40mm_HandSolder, F.Cu at (67.0, 260.6)
- added R63: 10k, Resistor_SMD:R_0805_2012Metric_Pad1.20x1.40mm_HandSolder, F.Cu at (67.0, 263.6)
- added R64: 5.6k, Resistor_SMD:R_0805_2012Metric_Pad1.20x1.40mm_HandSolder, F.Cu at (67.0, 266.6)
- added R65: 39k, Resistor_SMD:R_0805_2012Metric_Pad1.20x1.40mm_HandSolder, F.Cu at (67.0, 269.5)
- added R7: 18k, Resistor_SMD:R_0805_2012Metric_Pad1.20x1.40mm_HandSolder, F.Cu at (38.5, 124.2)
- added R8: 39k, Resistor_SMD:R_0805_2012Metric_Pad1.20x1.40mm_HandSolder, F.Cu at (40.5, 124.2)
- added R85: 100, Resistor_SMD:R_0805_2012Metric_Pad1.20x1.40mm_HandSolder, F.Cu at (80.4, 283.8)
- added R9: 39k, Resistor_SMD:R_0805_2012Metric_Pad1.20x1.40mm_HandSolder, F.Cu at (32.0, 130.7)
- J1: footprint Connector_Audio:Jack_6.35mm_Neutrik_NMJ4HCD2_Horizontal -> Custom_Footprints:Jack_6.35mm
- J4: footprint Connector_Audio:Jack_6.35mm_Neutrik_NMJ4HCD2_Horizontal -> Custom_Footprints:Jack_6.35mm; moved to B.Cu
- moved J4 189.7 mm to (155.4, 85.4)
- moved RV2 86.0 mm to (122.0, 104.2)
- moved RV1 62.0 mm to (101.0, 104.7)
- moved J1 22.7 mm to (45.7, 85.3), turned to 180 degrees
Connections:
- C45 pad 2: Net-(U8C--) -> Net-(U6C--)
- C48 pad 2: Net-(U9A--) -> Net-(U7A--)
- C50 pad 2: Net-(U9B--) -> Net-(U7B--)
- C52 pad 2: Net-(U9C--) -> Net-(U7C--)
- C54 pad 1: VCC4_5 -> Net-(U8D-+)
- C55 pad 2: VCC4_5 -> Net-(U8D-+)
- J1 pad T: Net-(C8-Pad1) -> Right jack
- J4 pad T: Net-(C9-Pad1) -> Left jack
- R69 pad 2: Net-(U9B--) -> Net-(U7B--)
- R72 pad 2: Net-(U9C--) -> Net-(U7C--)
- R83 pad 1: VCC4_5 -> Net-(U8D-+)
- R84 pad 2: VCC4_5 -> Net-(U8D-+)
- SW1 pad 1: unconnected-(SW1-A-Pad1) -> Left jack
- SW1 pad 2: unconnected-(SW1-B-Pad2) -> Net-(C9-Pad1)
- SW1 pad 3: unconnected-(SW1-C-Pad3) -> Right jack
- SW1 pad 4: unconnected-(SW1-A-Pad4) -> Left jack
- SW1 pad 5: unconnected-(SW1-B-Pad5) -> Net-(C8-Pad1)
- SW1 pad 6: unconnected-(SW1-C-Pad6) -> Right jack
- U2 pad 1: (no net) -> Net-(C11-Pad2)
- U2 pad 10: (no net) -> VCC4_5
- U2 pad 12: Net-(U2D-+) -> Vsig
- U2 pad 2: (no net) -> Net-(U2A--)
- U2 pad 3: (no net) -> VCC4_5
- U2 pad 5: (no net) -> VCC4_5
- U2 pad 6: (no net) -> Net-(U2B--)
- U2 pad 7: (no net) -> Net-(C13-Pad2)
- U2 pad 8: (no net) -> Net-(C15-Pad2)
- U2 pad 9: (no net) -> Net-(U2C--)
- U3 pad 1: (no net) -> Net-(C18-Pad2)
- U3 pad 10: (no net) -> VCC4_5
- U3 pad 12: Net-(U3D-+) -> Vsig
- U3 pad 2: (no net) -> Net-(U3A--)
- U3 pad 3: (no net) -> VCC4_5
- U3 pad 5: (no net) -> VCC4_5
- U3 pad 6: (no net) -> Net-(U3B--)
- U3 pad 7: (no net) -> Net-(C20-Pad2)
- U3 pad 8: (no net) -> Net-(C22-Pad2)
- U3 pad 9: (no net) -> Net-(U3C--)
- U6 pad 8: Net-(C29-Pad2) (its old number) -> Net-(C44-Pad2)
- U7 pad 1: Net-(C32-Pad2) (its old number) -> Net-(C47-Pad2)
- U7 pad 11: -5V -> GND
- U7 pad 7: Net-(C34-Pad2) (its old number) -> Net-(C49-Pad2)
- U7 pad 8: Net-(C36-Pad2) (its old number) -> Net-(C51-Pad2)
- U8 pad 1: Net-(C39-Pad2) (its old number) -> Net-(U8A--)
- U8 pad 11: (no net) -> GND
- U8 pad 12: Vsig -> Net-(U8D-+)
- U8 pad 13: Net-(U8D--) -> VCC4_5
- U8 pad 14: Net-(U8D--) -> VCC4_5
- U8 pad 3: VCC4_5 -> Net-(U8A-+)
- U8 pad 4: (no net) -> +9V
- U8 pad 5: VCC4_5 -> Net-(U8B-+)
- U8 pad 7: Net-(C41-Pad2) (its old number) -> Net-(U8B--)
- U8 pad 8: Net-(C44-Pad2) -> Net-(U8C--)
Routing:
- net Net-(C3-Pad2): track 0.00 -> 10.9 mm
- net Net-(C3-Pad1): track 0.00 -> 8.43 mm
- net Net-(C1-Pad1): track 0.00 -> 6.92 mm
- net Net-(C1-Pad2): track 0.00 -> 5.79 mm
- net Net-(U1A--): track 0.00 -> 2.96 mm
- net Net-(C5-Pad1): track 0.00 -> 2.83 mm
- net VCC4_5: track 0.00 -> 2.00 mm
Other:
- board text added: "LED Brightness"
- board text added: "Volume Range"
- board text removed: "LED Brightness Control"
- board text removed: "Volume Range Control"

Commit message: PCB V1 done
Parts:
- removed H3, H4: MountingHole, MountingHole:MountingHole_3.2mm_M3
- C1, C11, C12, C13, C14, C15, C16, C18, C19, C2, C20, C21, C22, C23, C25, C26, C27, C28, C29, C3, C30, C31, C32, C33, C34, C35, C36, C37, C38, C39, C4, C40, C41, C42, C44, C45, C5, C50, C51, C52, C53, C55, C56, C59, C6, C60, C61, C62, C63, C64, C65, C66, C67, C68, C69, C7, C70, C71, C72, C73, C74, C9: footprint Capacitor_SMD:C_0805_2012Metric_Pad1.18x1.45mm_HandSolder -> Custom_Footprints:C_0805_2012Metric_Pad1.18x1.45mm_HandSolder; moved to B.Cu
- C10, C17, C24, C54, C57, C58, C8, J3, J5, J6, TP1, TP10, TP11, TP12, TP13, TP14, TP2, TP3, TP4, TP5, TP6, TP7, TP8, TP9: moved to B.Cu
- C46, C47, C48, C49: footprint Capacitor_SMD:C_0805_2012Metric_Pad1.18x1.45mm_HandSolder -> Custom_Footprints:C_0805_2012Metric_Pad1.18x1.45mm_HandSolder
- R1, R10, R11, R12, R13, R14, R15, R16, R17, R18, R19, R2, R20, R21, R22, R23, R24, R25, R26, R27, R28, R29, R3, R30, R31, R32, R33, R34, R35, R36, R37, R38, R39, R4, R40, R41, R42, R43, R44, R45, R46, R47, R48, R49, R5, R50, R51, R52, R53, R54, R55, R56, R57, R58, R59, R6, R60, R61, R62, R63, R64, R65, R67, R68, R7, R73, R74, R8, R83, R84, R85, R9: footprint Resistor_SMD:R_0805_2012Metric_Pad1.20x1.40mm_HandSolder -> Custom_Footprints:R_0805_2012Metric_Pad1.20x1.40mm_HandSolder; moved to B.Cu
- R66, R69, R70, R71, R72, R75, R76, R77, R78, R79, R80, R81, R82: footprint Resistor_SMD:R_0805_2012Metric_Pad1.20x1.40mm_HandSolder -> Custom_Footprints:R_0805_2012Metric_Pad1.20x1.40mm_HandSolder
- RV1: value 10k_LED_Brightness_Pot -> 1k_LED_Brightness_Pot; footprint PTV09A_Pot_Vertical:PTV09 -> Potentiometer_THT:Potentiometer_Runtron_RM-065_Vertical
- RV2: footprint PTV09A_Pot_Vertical:PTV09 -> Potentiometer_THT:Potentiometer_Runtron_RM-065_Vertical
- moved Q1 256.7 mm to (49.7, 77.9), turned to 0 degrees
- moved R82 255.6 mm to (44.9, 74.7)
- moved D71 254.7 mm to (45.1, 78.9)
- moved C17 247.3 mm to (50.8, 40.3), turned to 90 degrees
- moved C24 245.0 mm to (71.2, 40.5), turned to 90 degrees
- moved C31 244.0 mm to (91.3, 40.5), turned to 90 degrees
- moved C38 243.8 mm to (111.2, 40.6), turned to 90 degrees
- moved C20 239.2 mm to (65.6, 58.3)
- moved C41 239.0 mm to (125.5, 58.3)
- moved C39 238.6 mm to (131.9, 54.7), turned to 90 degrees
- moved C42 238.2 mm to (121.3, 60.9), turned to 90 degrees
- moved C27 238.2 mm to (85.6, 58.3)
- moved C34 238.0 mm to (105.5, 58.3)
- moved C28 237.9 mm to (81.4, 60.9), turned to 90 degrees
- moved C35 237.6 mm to (101.3, 60.9), turned to 90 degrees
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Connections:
- J2 pad 2: Net-(J2-GNDBREAK) -> Net-(J2-GND)
- J2 pad 3: Net-(J2-GND) -> Net-(J2-GNDBREAK)
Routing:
- net GND: track 0.00 -> 744.2 mm, vias 0 -> 2
- net VCC4_5: track 2.00 -> 413.4 mm, vias 0 -> 12
- net +9V: track 379.7 -> 778.0 mm, vias 0 -> 11
- net LED_Brightness_Control: track 0.00 -> 236.4 mm, vias 0 -> 2
- net Vsig: track 0.00 -> 222.1 mm, vias 0 -> 7
- net Mode: track 0.00 -> 217.2 mm
- net Rhi_Value: track 0.00 -> 197.1 mm, vias 0 -> 2
- net Right jack: track 0.00 -> 71.2 mm
- net Net-(U8A-+): track 0.00 -> 60.3 mm, vias 0 -> 1
- net Net-(J5-Pin_1): track 0.00 -> 57.1 mm
- net Left jack: track 0.00 -> 53.5 mm
- net Net-(C29-Pad2): track 0.00 -> 46.5 mm, vias 0 -> 1
- net Net-(C36-Pad2): track 0.00 -> 43.8 mm, vias 0 -> 1
- net Net-(C15-Pad2): track 0.00 -> 40.3 mm, vias 0 -> 1
- net Net-(C51-Pad2): track 0.00 -> 40.2 mm, vias 0 -> 1
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- added copper zone on B.Cu, net GND
- added copper zone on F.Cu, net GND
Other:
- board size 295 x 155 mm -> 141.4 x 82 mm
- board text added: "11"
- board text added: "12"
- board text removed: "GND"
- board text removed: "Power"
- board text removed: "SIG"

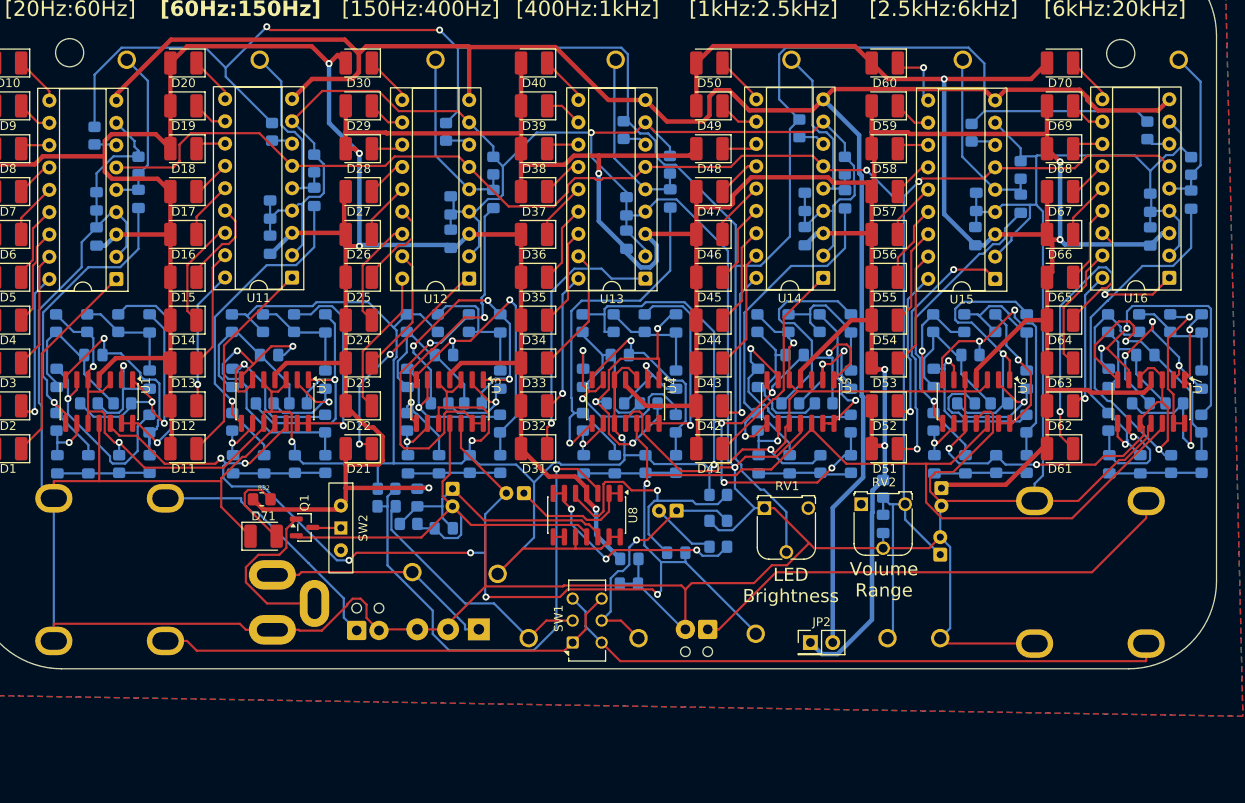
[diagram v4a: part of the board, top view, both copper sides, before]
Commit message: Fix jack reverse
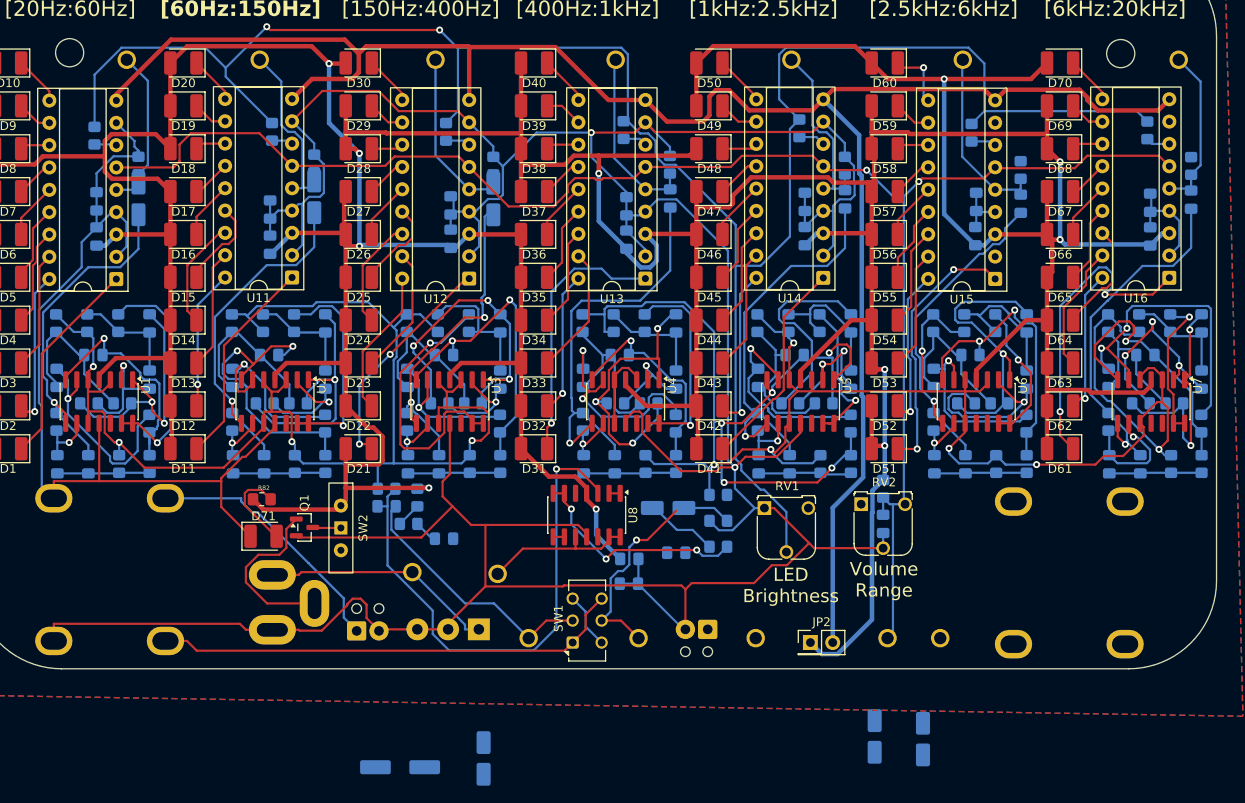
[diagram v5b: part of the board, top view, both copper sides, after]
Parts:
- C10, C57, C58, C8: footprint Capacitor_THT:CP_Radial_D5.0mm_P2.00mm -> Capacitor_SMD:CP_Elec_4x5.4
- C17, C24, C43: footprint Capacitor_SMD:C_0805_2012Metric_Pad1.18x1.45mm_HandSolder -> Capacitor_SMD:CP_Elec_4x5.4
- C54: footprint Capacitor_THT:CP_Radial_D5.0mm_P2.00mm -> Capacitor_SMD:CP_Elec_6.3x5.3
- moved C54 32.2 mm to (60.6, 105.2), turned to 0 degrees
- moved C10 30.5 mm to (70.1, 104.2), turned to 90 degrees
- moved C58 29.3 mm to (114.6, 101.7)
- moved J1 22.2 mm to (130.4, 91.2), turned to 0 degrees
- moved C57 21.1 mm to (120.1, 102.0)
- moved C55 1.19 mm to (65.6, 79.2)
- moved C8 1.02 mm to (91.1, 75.7)
- moved TP9 0.50 mm to (101.1, 90.5)
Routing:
- net Vsig: track 222.1 -> 0.00 mm, vias 7 -> 0
- net GND: track 744.2 -> 555.2 mm
- net Right jack: track 71.2 -> 6.37 mm
- net Net-(J5-Pin_1): track 57.1 -> 0.00 mm
- net VCC4_5: track 413.4 -> 374.1 mm, vias 12 -> 11
- net Net-(U8B-+): track 31.6 -> 0.00 mm, vias 1 -> 0
- net Net-(U8D-+): track 30.2 -> 2.83 mm
- net +9V: track 778.0 -> 763.4 mm
- net Net-(U8A--): track 14.7 -> 1.27 mm
- net Rhi_Value: track 197.1 -> 189.7 mm
- net Net-(C8-Pad2): track 7.44 -> 8.33 mm
- net Net-(C8-Pad1): track 28.3 -> 27.6 mm
